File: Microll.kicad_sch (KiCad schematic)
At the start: 16 parts, among them J1 USB_C_Receptacle, U1 ESP32-C3-WROOM-02-N4, U2 TLV76733DRVx, U3 STM32G0B1CBU6, U4 USBLC6-2P6, U5 DPDT_Switch_x2, U6 LSM6DSL

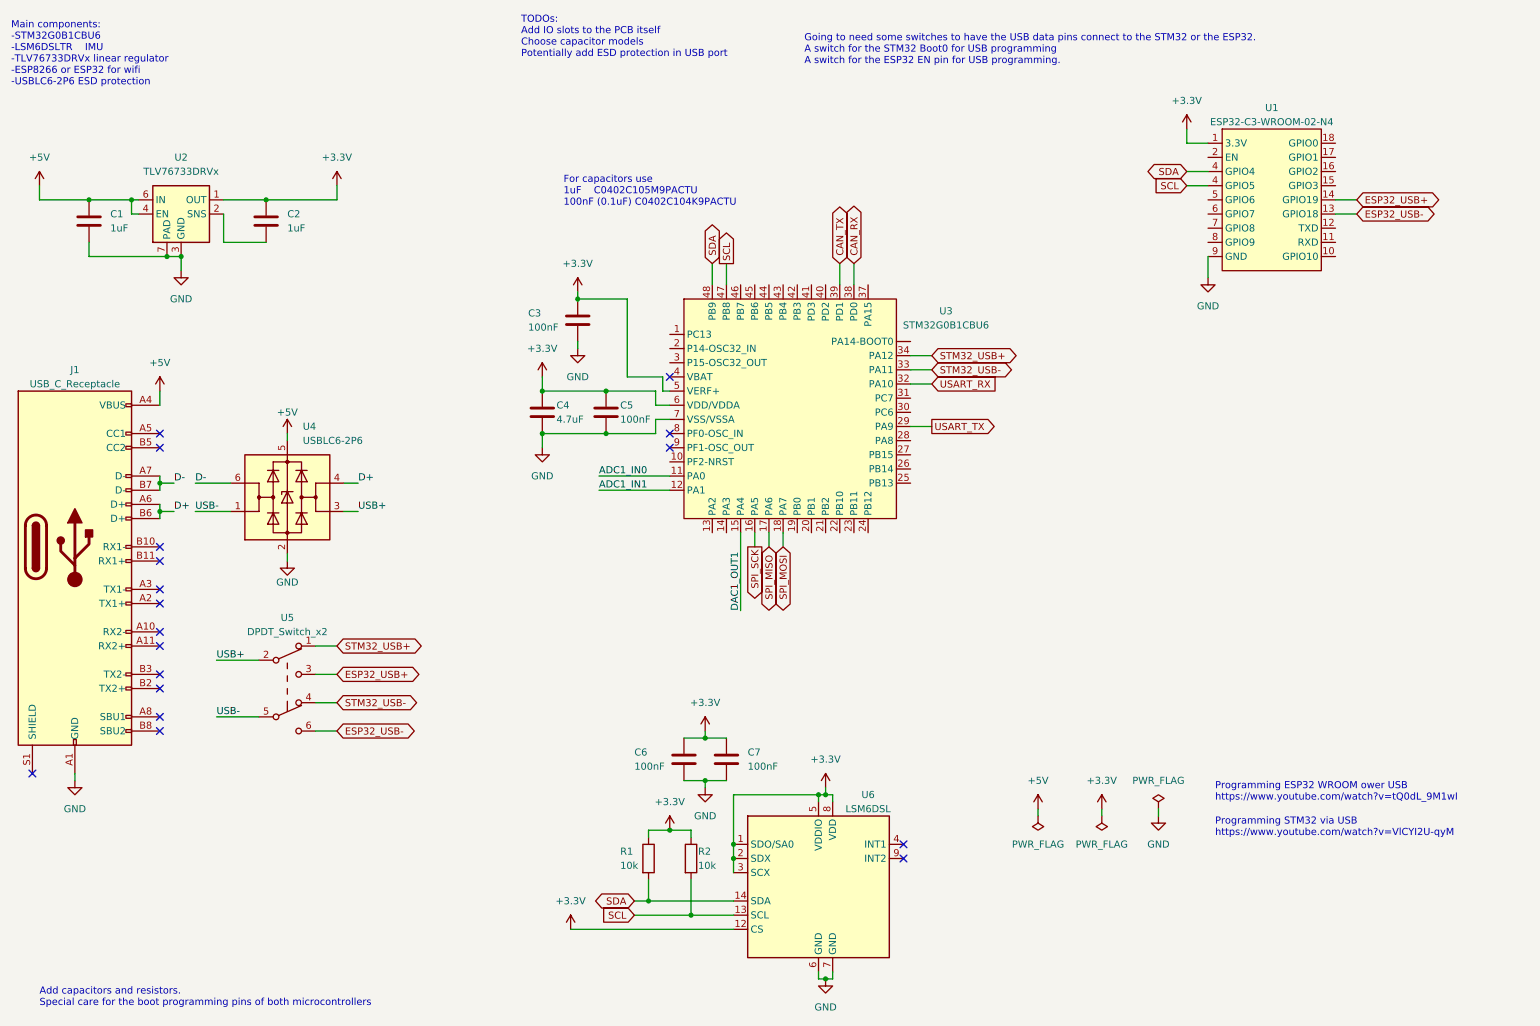
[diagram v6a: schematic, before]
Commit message: Added an RGB LED and solder jumpers for the EN and Boot pins of the microcontrollers in case I need to do something woth programming
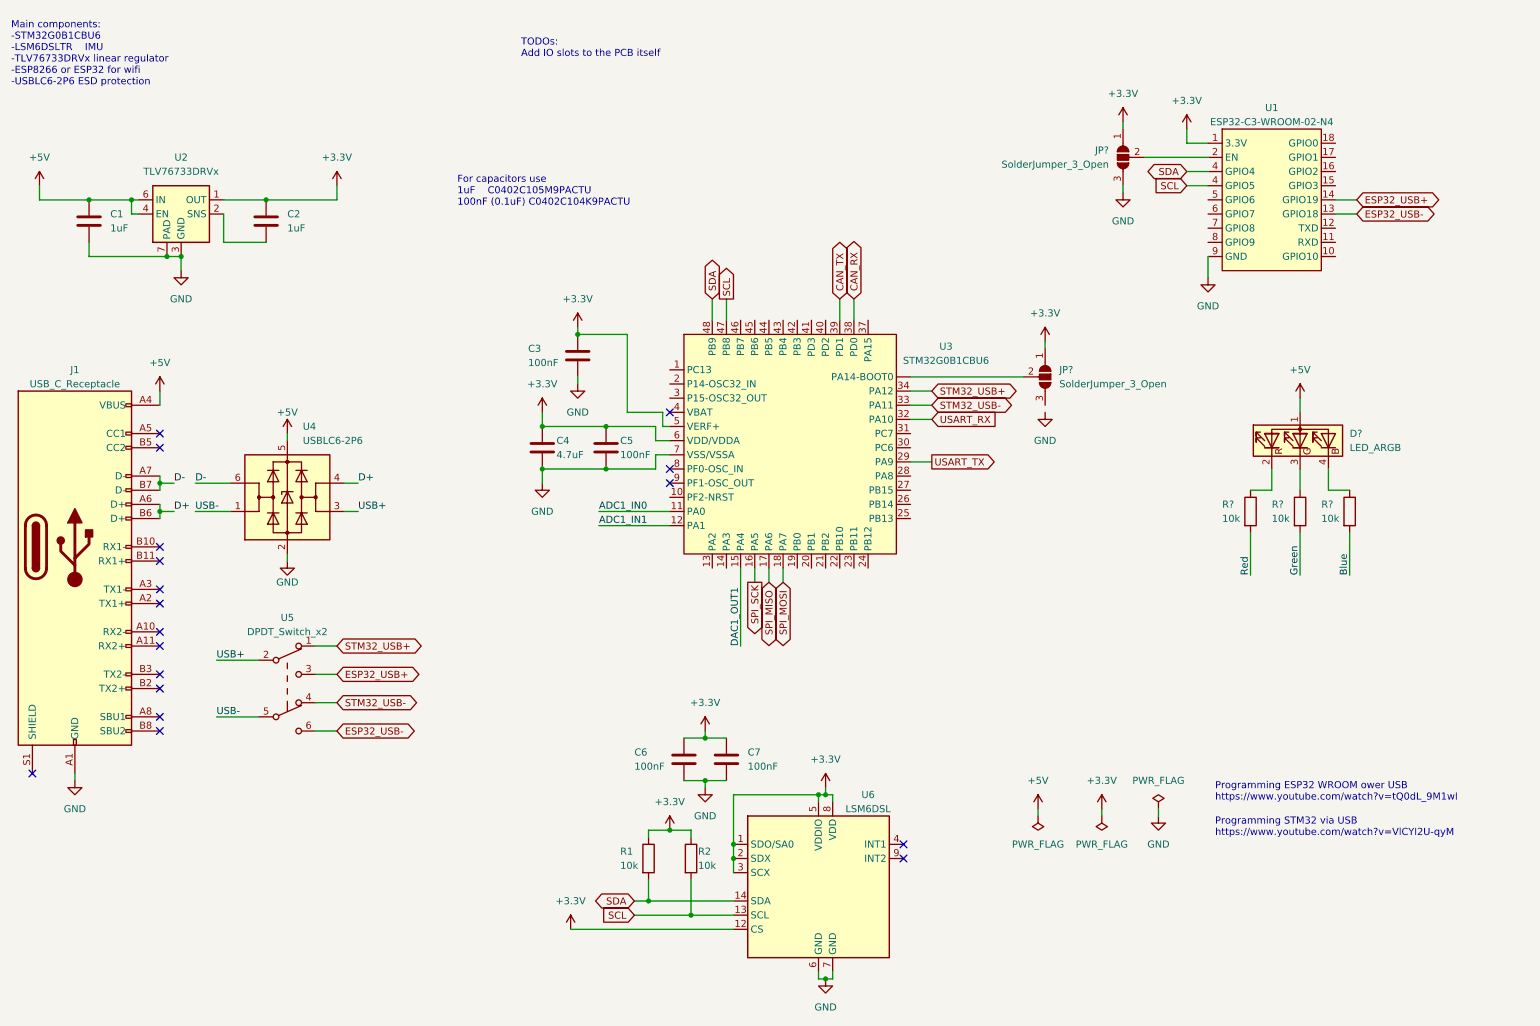
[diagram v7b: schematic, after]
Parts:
- added D?: LED_ARGB, RGB_LED:APTF1616LSEEZGKQBKC, symbol Device:LED_ARGB
- added JP? (x2): SolderJumper_3_Open, symbol Jumper:SolderJumper_3_Open
- added R? (x3): 10k, Resistor_SMD:R_0402_1005Metric, symbol Device:R
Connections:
- net +3.3V: now also JP?.1 (A), JP?.1 (A)
- net +5V: now also D?.1 (A)
- net GND: now also JP?.3 (B)
- net at U1.2 (EN): now also JP?.2 (C)
- net at U3. (PA14-BOOT0): now also JP?.2 (C)
- new net: D?.2 (RK), R?.1
- new net: D?.3 (GK), R?.1
- new net: D?.4 (BK), R?.1
- new net Blue: R?.2
- new net Green: R?.2
- new net Red: R?.2
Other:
- note added: "TODOs: Add IO slots to the PCB itself"
- note removed: "Add capacitors and resistors. Special care for the boot programming pins of both microcontrollers"
- note removed: "Going to need some switches to have the USB data pins connect to the STM32 or the ESP32. A switch for the STM32 Boot0 for USB programming A switch for the ESP32 EN pin for USB programming."
- note removed: "TODOs: Add IO slots to the PCB itself Choose capacitor models Potentially add ESD protection in USB port"
- moved on the sheet: C3, C4, C5, U3

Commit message: Added nets to the LEDs. Pretty much all that is left in the scematic is adding the I/O pins and then it's off to the PCB layout
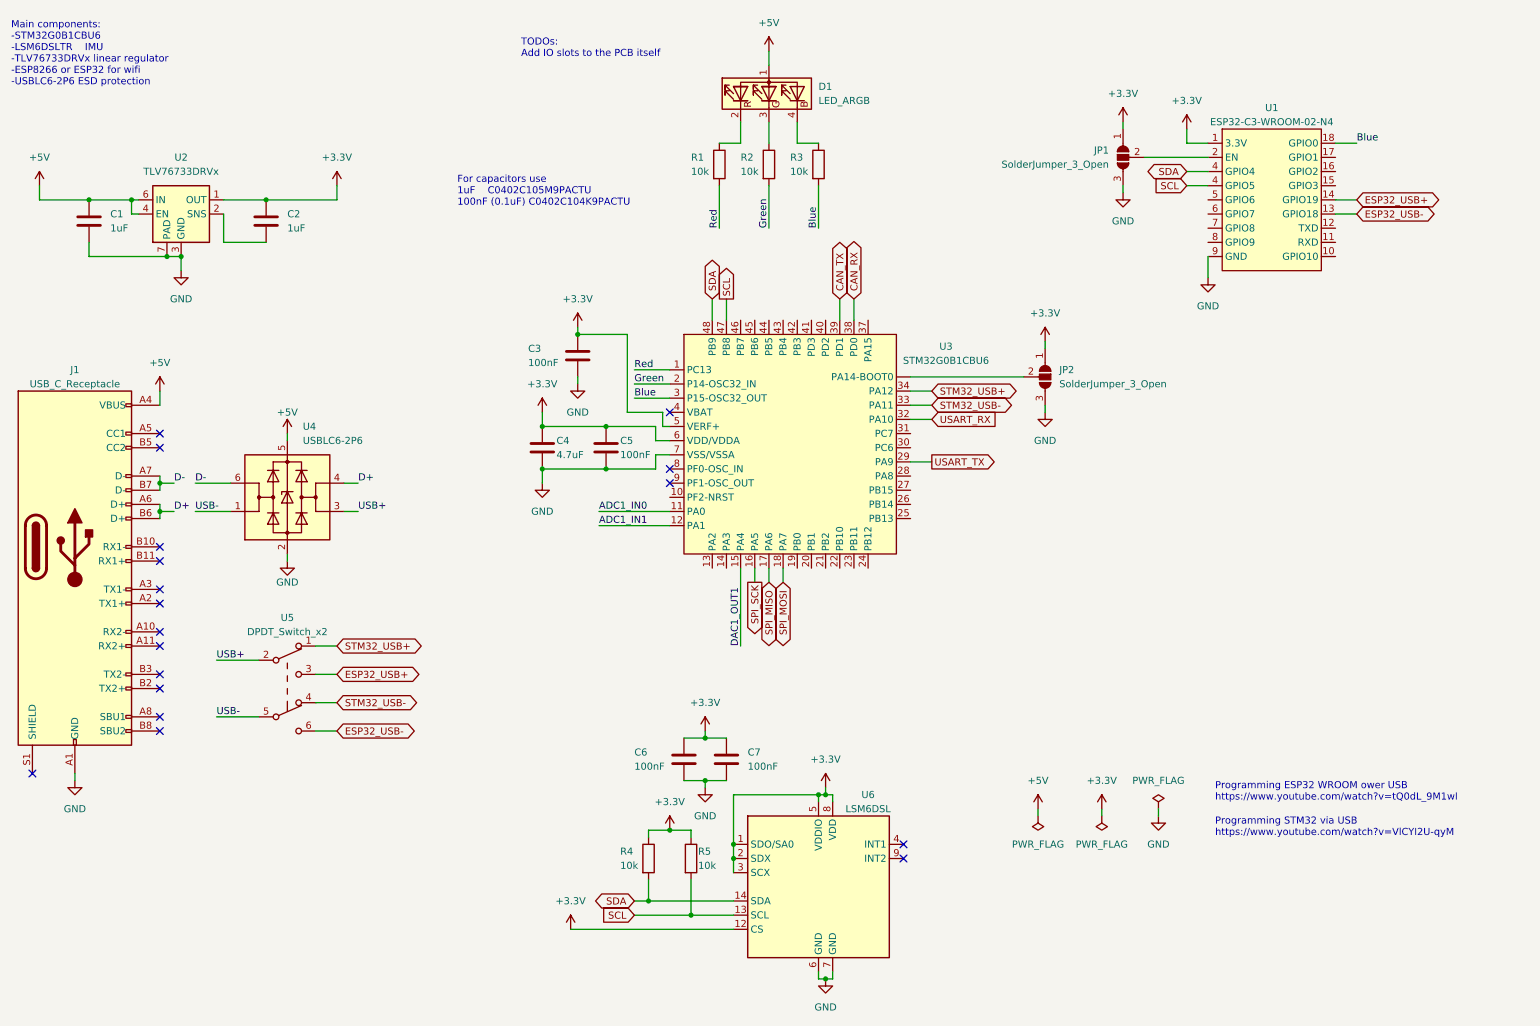
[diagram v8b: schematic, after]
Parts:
- JP1, JP2: renamed from JP?; footprint (none) -> Jumper:SolderJumper-3_P1.3mm_Open_RoundedPad1.0x1.5mm_NumberLabels
- gave numbers to parts that had none: 4
- renumbered R1 to R4, R2 to R5
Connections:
- net Blue: now also U1.18 (GPIO0), U3.3 (P15-OSC32_OUT)
- net GND: now also JP2.3 (B)
- net Green: now also U3.2 (P14-OSC32_IN)
- net Red: now also U3.1 (PC13)
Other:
- moved on the sheet: D1, R1, R2, R3
